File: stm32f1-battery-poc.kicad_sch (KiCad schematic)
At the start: 118 parts, among them J1 Conn_02x07_Odd_Even, J2 Conn_01x02, J3 Conn_01x02, M1 Motor_3_Phases, Q1 Q_NMOS, Q2 Q_NMOS, SW1 SW_Push, SW2 SW_Push, SW3 SW_Push, SW4 SW_SPST, U1 STM32F103C8Tx, U2 SN65HVD230, U3 BQ77905, U4 LM78M05, U5 HT753-1, U6 DRV8311H, U7 QRE1113GR, U8 QRE1113GR, U9 QRE1113GR, Y1 8M

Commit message: schem: run and fix ERC
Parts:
- removed TP2: TestPoint, symbol Connector:TestPoint
- added C37: 0u1, symbol Device:C
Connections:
- net +3V3: now also U1.1 (VBAT), C37.1
- net EPAD: now also C37.2
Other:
- moved on the sheet: C3, C4, C5, C6, D6, R23

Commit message: schem: reannotate
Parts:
- renumbered BT3 to BT1, BT1 to BT3, C36 to C1, C25 to C10, C26 to C11, C28 to C12, C30 to C13, C27 to C14, C29 to C15, C6 to C16, C7 to C17, C5 to C18, C8 to C19, C20 to C2, C9 to C20, C4 to C21, C3 to C22, C37 to C23, C1 to C24, C2 to C25, C16 to C26, C18 to C27, C13 to C28, C11 to C29, C22 to C3, C12 to C30, C17 to C34, C15 to C35, C19 to C36, C14 to C37, C35 to C4, C34 to C5, C10 to C6, C24 to C7, C21 to C8, C23 to C9, D6 to D1, D7 to D2, D5 to D3, D3 to D4, D1 to D5, D4 to D6, D2 to D7, FB2 to FB1, FB1 to FB2, J2 to J1, J1 to J2, JP2 to JP1, JP3 to JP2, JP4 to JP3, JP1 to JP4, R24 to R1, R28 to R10, R29 to R11, R30 to R12, R8 to R13, R21 to R14, R9 to R15, R10 to R16, R20 to R17, R31 to R18, R32 to R19, R4 to R2, R33 to R20, R13 to R21, R17 to R23, R14 to R24, R18 to R25, R16 to R26, R12 to R27, R19 to R28, R15 to R29, R5 to R3, R11 to R30, R3 to R4, R23 to R5, R1 to R6, R2 to R7, R6 to R8, R7 to R9, SW4 to SW3, SW3 to SW4, TP11 to TP1, TP4 to TP10, TP8 to TP11, TP7 to TP12, TP6 to TP13, TP5 to TP14, TP12 to TP2, TP14 to TP3, TP10 to TP4, TP13 to TP5, TP9 to TP6, TP1 to TP7, TP15 to TP8, TP3 to TP9, U4 to U1, U5 to U2, U2 to U3, U6 to U4, U1 to U5, U7 to U6, U8 to U7, U9 to U8, U3 to U9

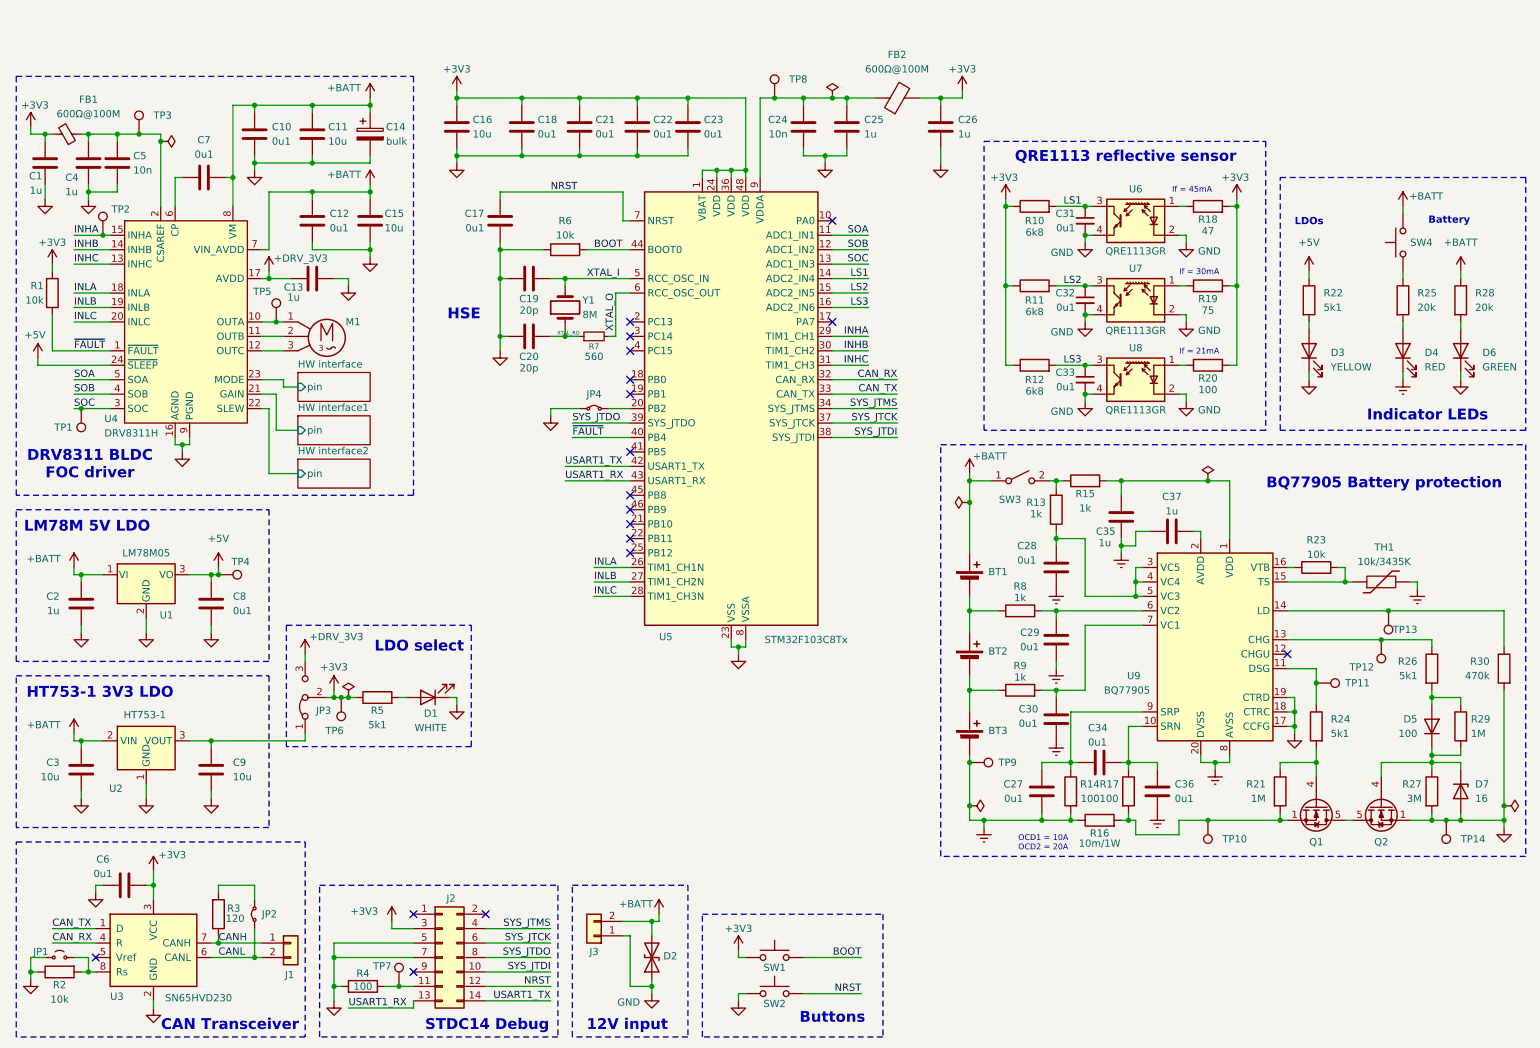
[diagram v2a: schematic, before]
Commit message: schem: regorganize to leave space for DRV8424RGER
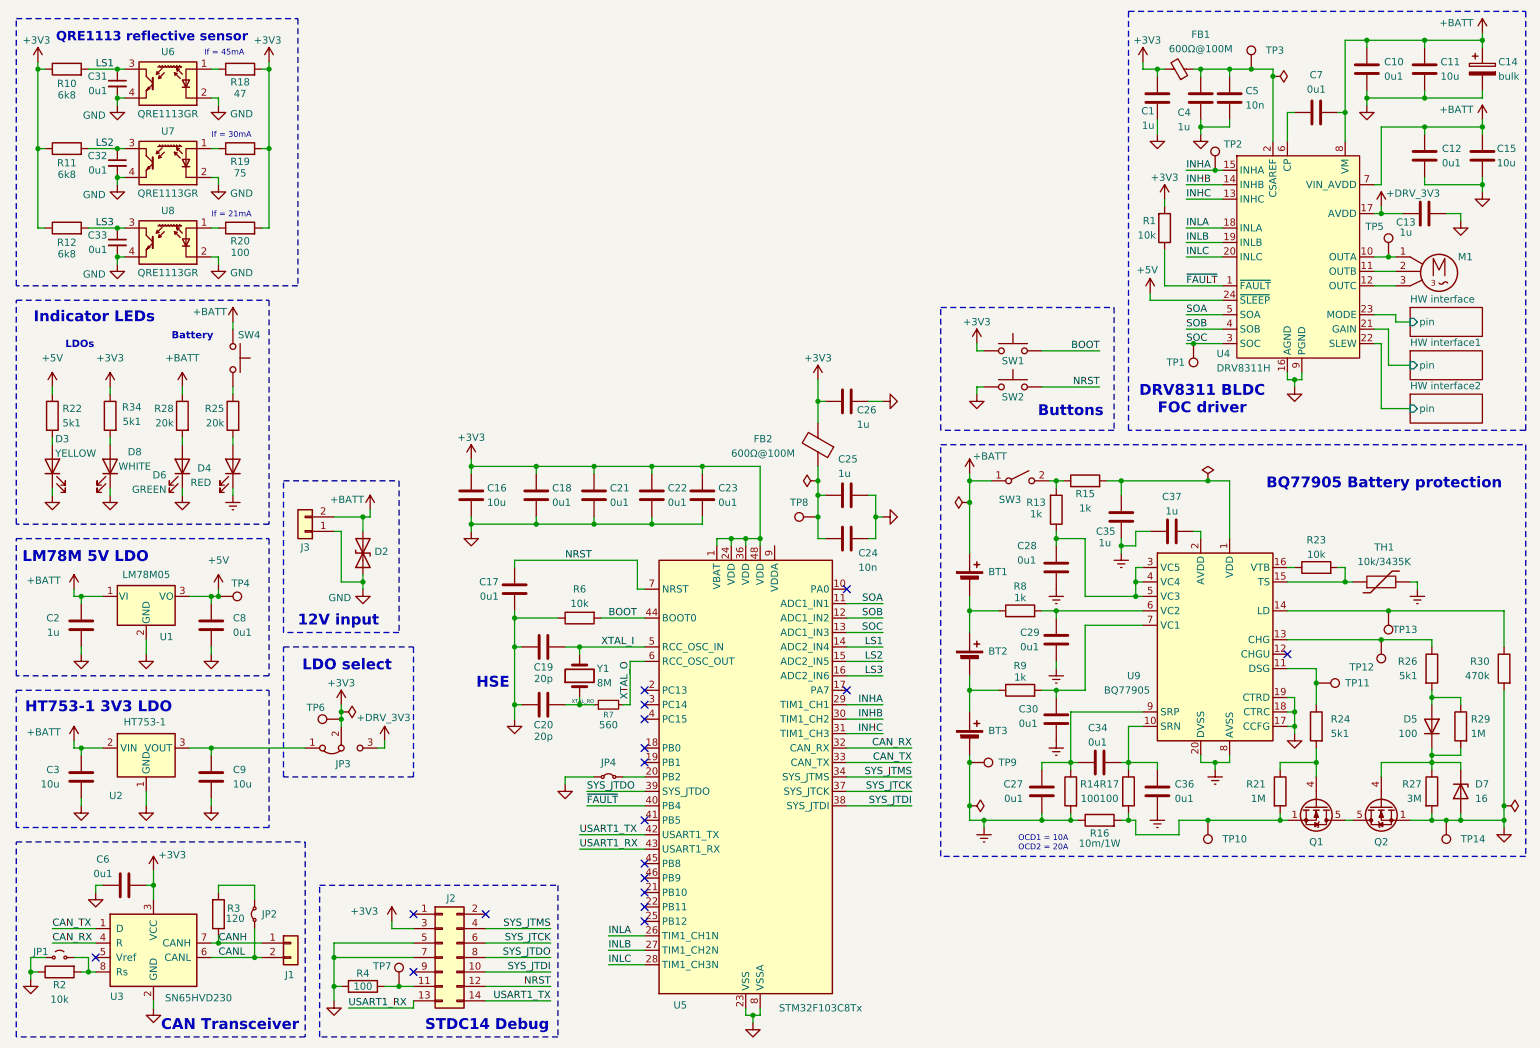
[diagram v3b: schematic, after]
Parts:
- removed D1: WHITE, LED_SMD:LED_0603_1608Metric, symbol Device:LED
- removed R5: 5k1, Resistor_SMD:R_0402_1005Metric, symbol Device:R
- added D8: WHITE, LED_SMD:LED_0603_1608Metric, symbol Device:LED
- added R34: 5k1, Resistor_SMD:R_0402_1005Metric, symbol Device:R
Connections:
- net +3V3: now also R34.1
- net EPAD: now also D8.1 (K)
- net at C24.1, C25.1, FB2.1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: no longer U5.9 (VDDA)
- new net: D8.2 (A), R34.2
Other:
- moved on the sheet: C1, C10, C11, C12, C13, C14, C15, C16, C17, C18, C19, C2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

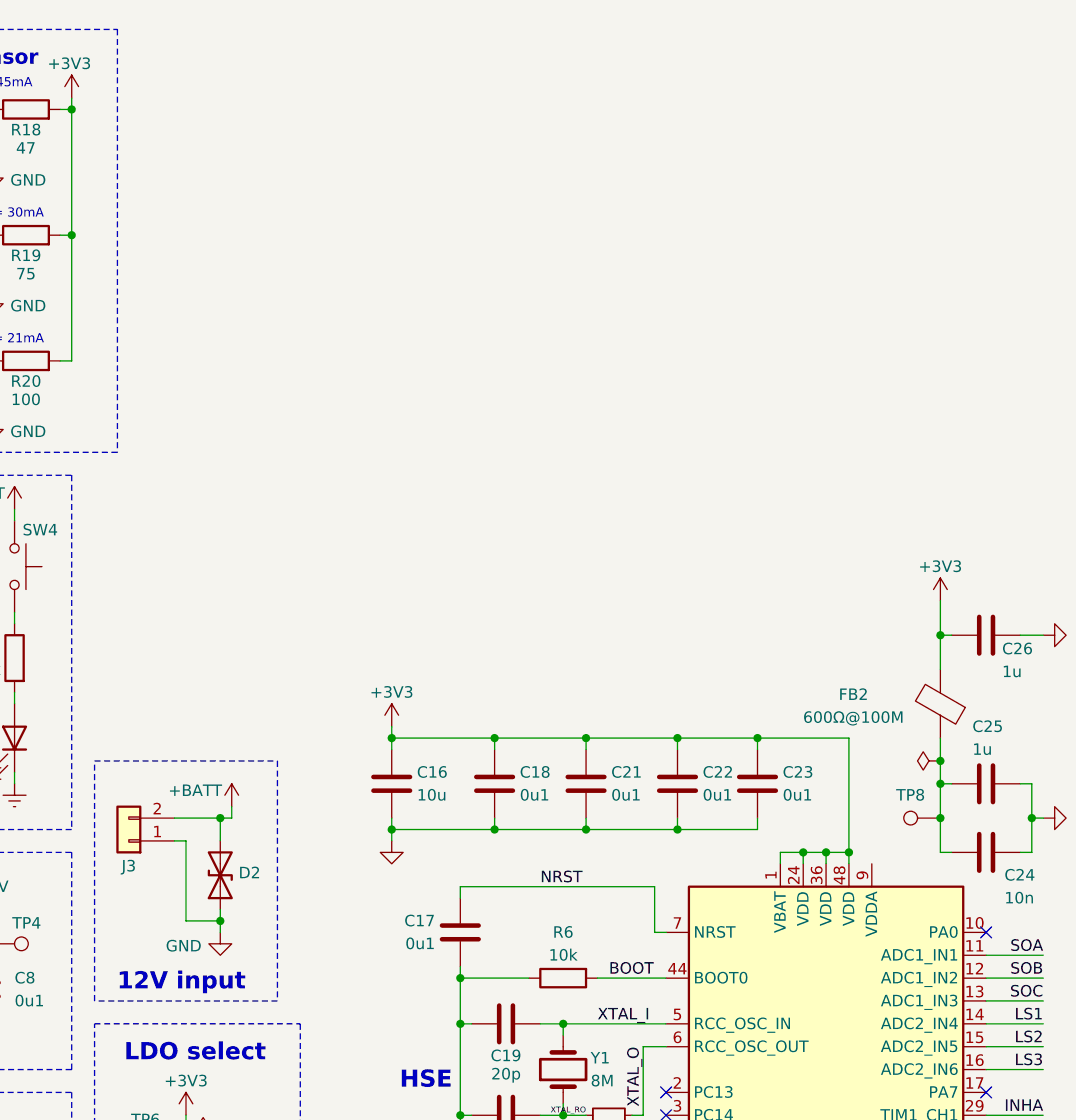
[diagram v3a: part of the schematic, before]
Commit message: schem: add DRV8424RGER stepper driver
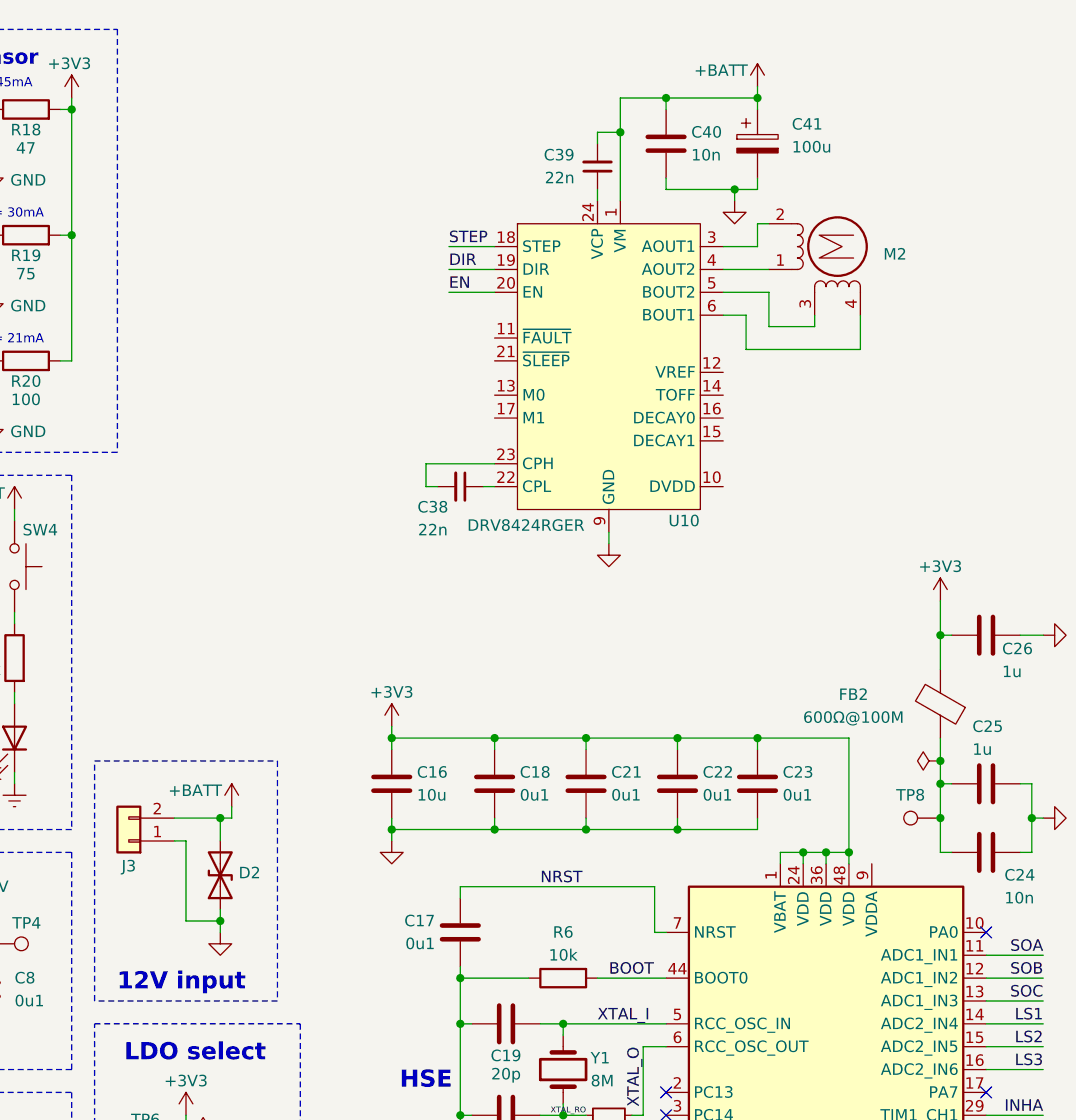
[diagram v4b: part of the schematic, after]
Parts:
- added C38, C39: 22n, symbol Device:C_Small
- added C40: 10n, symbol Device:C
- added C41: 100u, symbol Device:C_Polarized
- added M2: Stepper_Motor_bipolar, symbol Motor:Stepper_Motor_bipolar
- added U10: DRV8424RGER, GLCS:Texas_RGE0024B_VQFN-24-1EP_4x4mm_P0.5mm_EP2.5x2.5mm_ThermalVias, symbol GLCS:DRV8424RGER
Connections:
- net +BATT: now also C39.2, C40.1, C41.1, U10.1 (VM), U10.8 (VM)
- net EPAD: now also C40.2, C41.2, U10.2 (PGND), U10.25 (GND), U10.7 (PGND), U10.9 (GND)
- new net: M2.1, U10.4 (AOUT2)
- new net: M2.2 (-), U10.3 (AOUT1)
- new net: M2.3, U10.5 (BOUT2)
- new net: M2.4, U10.6 (BOUT1)
- new net: C38.1, U10.22 (CPL)
- new net: C38.2, U10.23 (CPH)
- new net: C39.1, U10.24 (VCP)
- new net DIR: U10.19 (DIR)
- new net EN: U10.20 (EN)
- new net STEP: U10.18 (STEP)

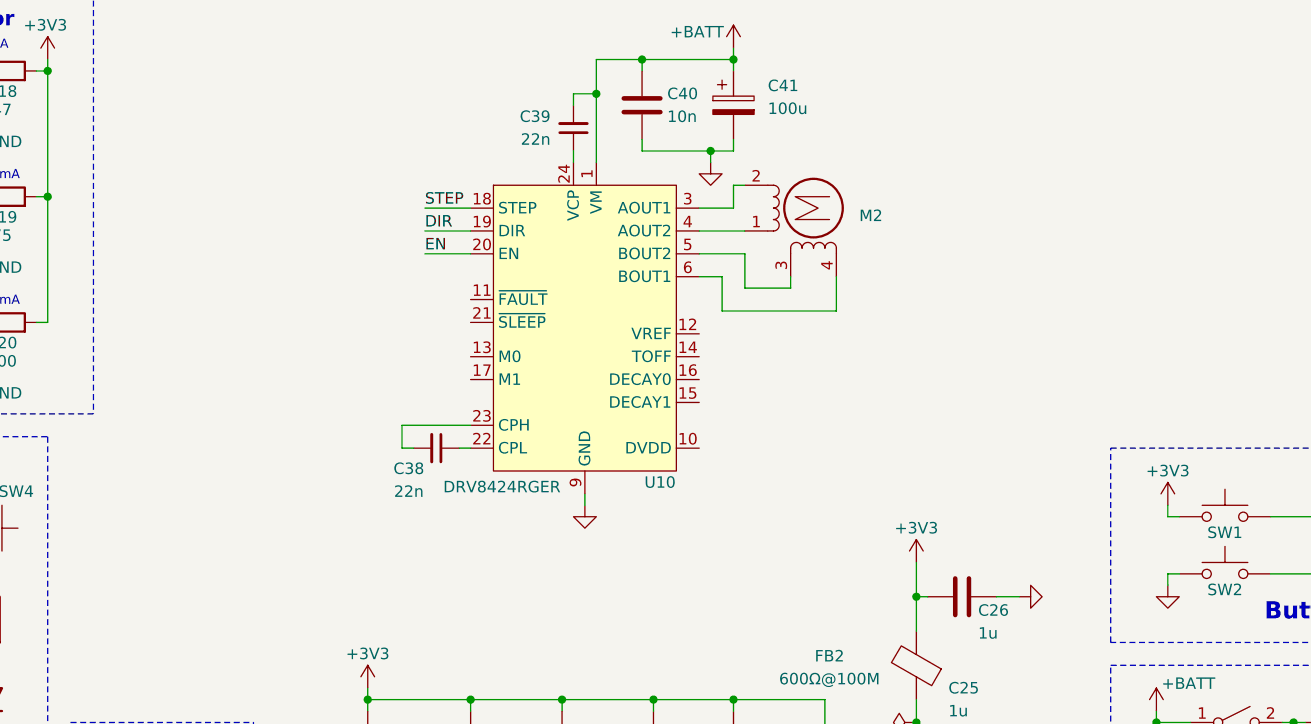
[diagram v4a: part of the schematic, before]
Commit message: schem: add DRV8424 mode setting jumpers
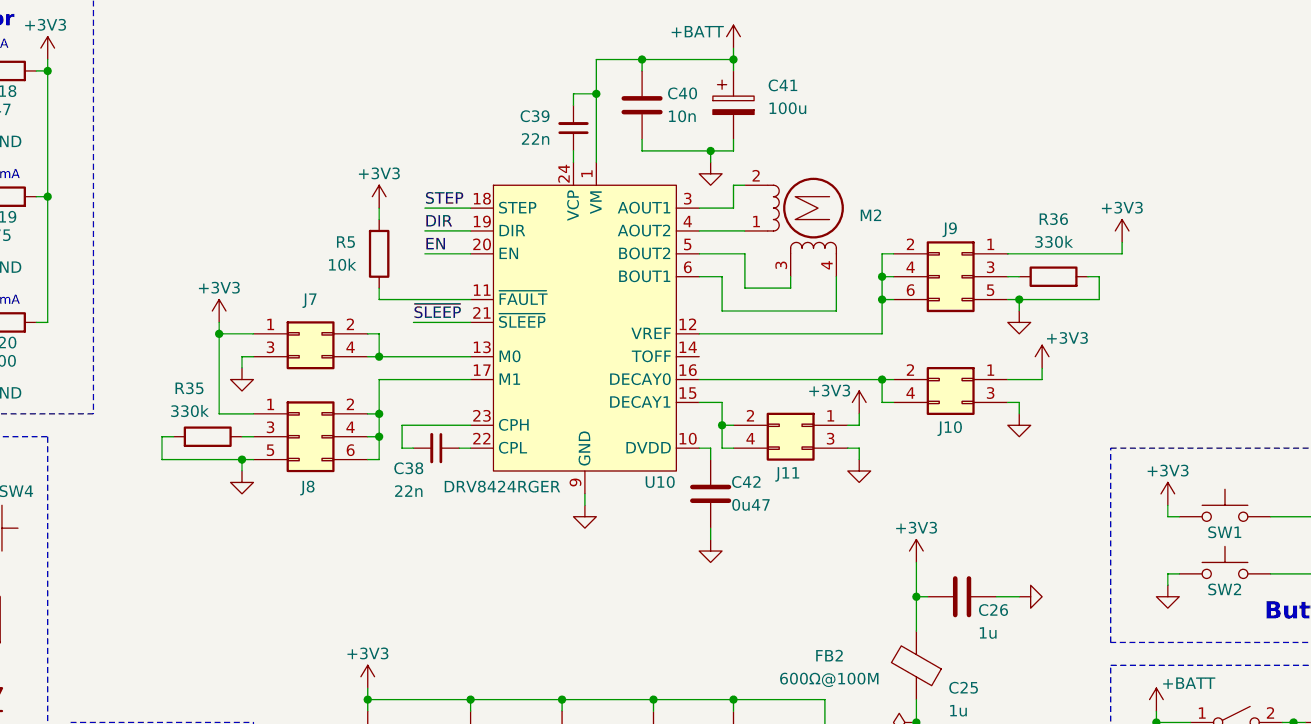
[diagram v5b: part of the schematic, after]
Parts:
- added C42: 0u47, symbol Device:C
- added J10, J11, J7: Conn_02x02_Odd_Even, symbol Connector_Generic:Conn_02x02_Odd_Even
- added J8, J9: Conn_02x03_Odd_Even, symbol Connector_Generic:Conn_02x03_Odd_Even
- added R35, R36: 330k, symbol Device:R
- added R5: 10k, symbol Device:R
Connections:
- net +3V3: now also J10.1 (Pin_1), J11.1 (Pin_1), J7.1 (Pin_1), J8.1 (Pin_1), J9.1 (Pin_1), R5.2
- net EPAD: now also C42.2, J10.3 (Pin_3), J11.3 (Pin_3), J7.3 (Pin_3), J8.5 (Pin_5), J9.5 (Pin_5), R35.2, R36.2
- net at U10.10 (DVDD): now also C42.1
- net at U10.11 (~{FAULT}): now also R5.1
- net at U10.12 (VREF): now also J9.2 (Pin_2), J9.4 (Pin_4), J9.6 (Pin_6)
- net at U10.13 (M0): now also J7.2 (Pin_2), J7.4 (Pin_4)
- net at U10.15 (DECAY1): now also J11.2 (Pin_2), J11.4 (Pin_4)
- net at U10.16 (DECAY0): now also J10.2 (Pin_2), J10.4 (Pin_4)
- net at U10.17 (M1): now also J8.2 (Pin_2), J8.4 (Pin_4), J8.6 (Pin_6)
- net ~{SLEEP}: now reaches U10.21 (~{SLEEP})
- new net: J8.3 (Pin_3), R35.1
- new net: J9.3 (Pin_3), R36.1
